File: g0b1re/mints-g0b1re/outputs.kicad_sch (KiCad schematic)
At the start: 46 parts, among them Q201 DMP3050LVT-7, Q202 DMP3050LVT-7, Q203 DMP3050LVT-7, Q204 DMP3050LVT-7, Q205 DMP3050LVT-7, Q206 DMP3050LVT-7, Q207 DMP3050LVT-7, Q208 DMP3050LVT-7, U201 140357145200, U202 140357145200, U203 140357145200, U204 140357145200, U205 140357145200, U206 140357145200, U207 140357145200, U208 140357145200

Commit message: notes from DR
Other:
- note added: "Add aux power LED"
- note added: "pick better fet P channel MOSFET 60v 15A lowest on resistance you can"
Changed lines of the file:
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@@
+		)
+	)
+	(text "Add aux power LED"
+		(exclude_from_sim no)
+		(at 270.256 78.74 0)
+		(effects
+			(font
+				(size 1.27 1.27)
+				(color 255 29 20 1)
+			)
 		)
 	)
@@
 			(font
 				(size 1.27 1.27)
+			)
+		)
+	)
+	(text "pick better fet\nP channel MOSFET\n60v 15A\nlowest on resistance you can"
+		(exclude_from_sim no)
+		(at 195.58 46.99 0)
+		(effects
+			(font
+				(size 1.27 1.27)
+				(color 255 25 18 1)
 			)
 		)
@@
 			(justify left bottom)
 		)
-		(property "Netclass" "iso_power"
+		(property "Net Class" "iso_power"
 			(at 309.8165 76.47 0)
 			(show_name no)
@@
 			(justify left bottom)
 		)
-		(property "Netclass" "data"
+		(property "Net Class" "data"
 			(at 119.3165 61.23 0)
 			(show_name no)
@@
 			(justify left bottom)
 		)
-		(property "Netclass" "data"
+		(property "Net Class" "data"
 			(at 119.3165 145.05 0)
 			(show_name no)
@@
 			(justify left bottom)
 		)
-		(property "Netclass" "data"
+		(property "Net Class" "data"
 			(at 119.3165 103.14 0)
 			(show_name no)
@@
 			(justify left bottom)
 		)
-		(property "Netclass" "iso_power"
+		(property "Net Class" "iso_power"
 			(at 288.2265 79.01 0)
 			(show_name no)
@@
 			(justify left bottom)
 		)
-		(property "Netclass" "data"
+		(property "Net Class" "data"
 			(at 119.3165 81.55 0)
 			(show_name no)
@@
 			(justify left bottom)
 		)
-		(property "Netclass" "data"
+		(property "Net Class" "data"
 			(at 119.3165 165.37 0)
 			(show_name no)
@@
 			(justify left bottom)
 		)
-		(property "Netclass" "iso_power"
+		(property "Net Class" "iso_power"
 			(at 288.2265 76.47 0)
 			(show_name no)
@@
 			(justify left bottom)
 		)
-		(property "Netclass" "data"
+		(property "Net Class" "data"
 			(at 119.3165 186.96 0)
 			(show_name no)
@@
 			(justify left bottom)
 		)
-		(property "Netclass" "data"
+		(property "Net Class" "data"
 			(at 119.3165 123.46 0)
 			(show_name no)
@@
 			(justify left bottom)
 		)
-		(property "Netclass" "data"
+		(property "Net Class" "data"
 			(at 119.3165 207.28 0)
 			(show_name no)

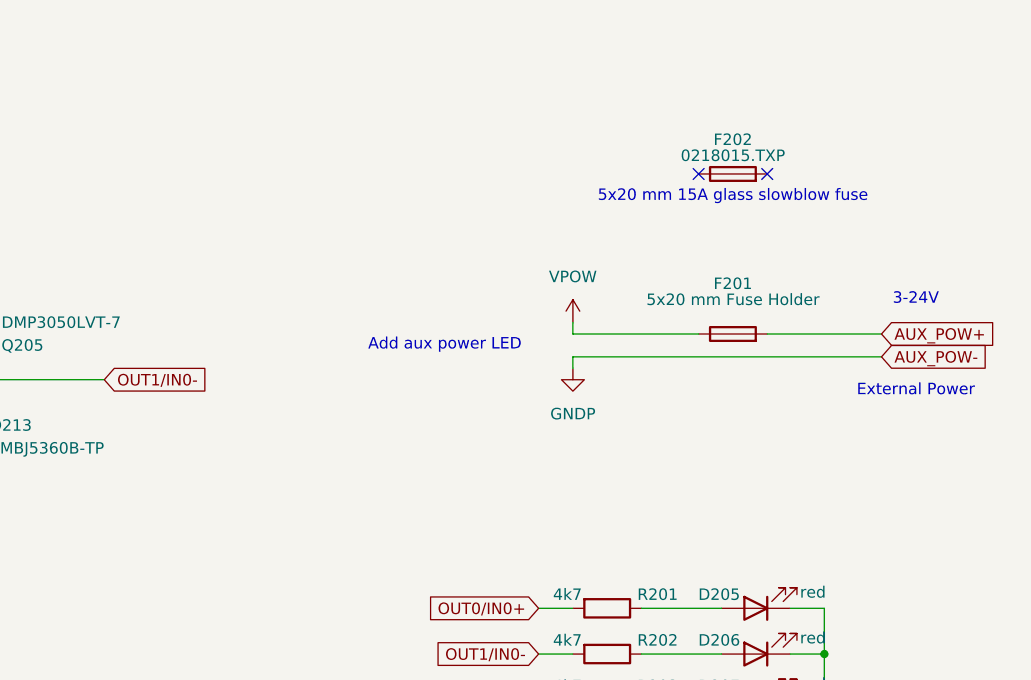
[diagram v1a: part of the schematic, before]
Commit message: post board review schmatic updates
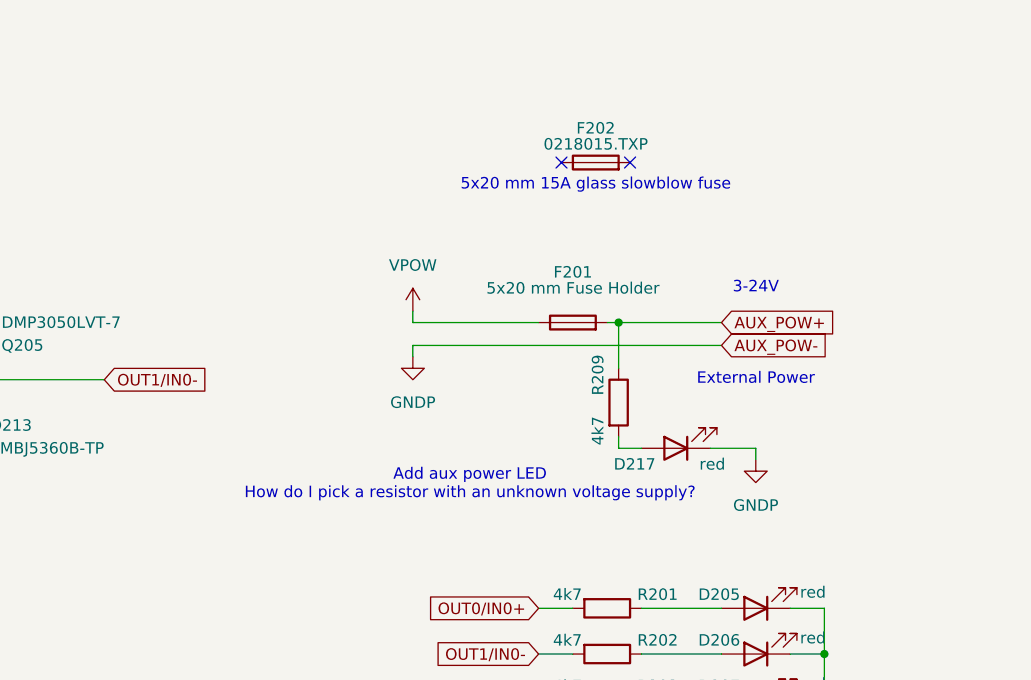
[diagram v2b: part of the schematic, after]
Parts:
- added D217: red, LED_SMD:LED_0603_1608Metric, symbol Device:LED
- added R209: 4k7, Resistor_SMD:R_0603_1608Metric, symbol Device:R
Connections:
- net AUX_POW+: now also R209.1
- net GNDP: now also D217.1 (K)
- new net: D217.2 (A), R209.2
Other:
- note added: "Add aux power LED How do I pick a resistor with an unknown voltage supply?"
- note removed: "Add aux power LED"
- moved on the sheet: F201, F202

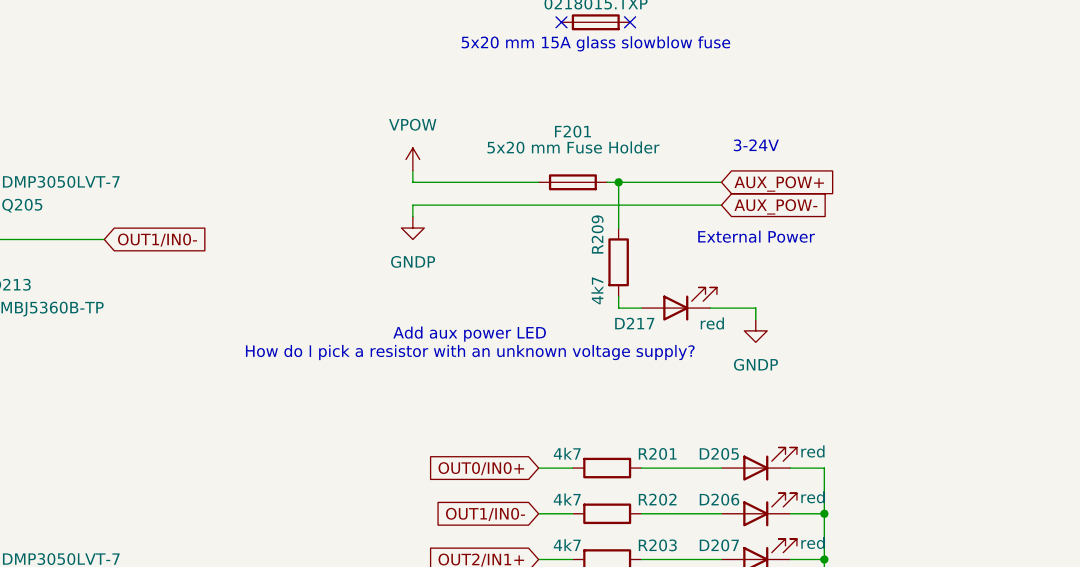
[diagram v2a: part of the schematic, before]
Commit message: Schematic progress
Swapped s2c chip, changed 8 pin connecters out with 4 pin, added test
point, removed net labels
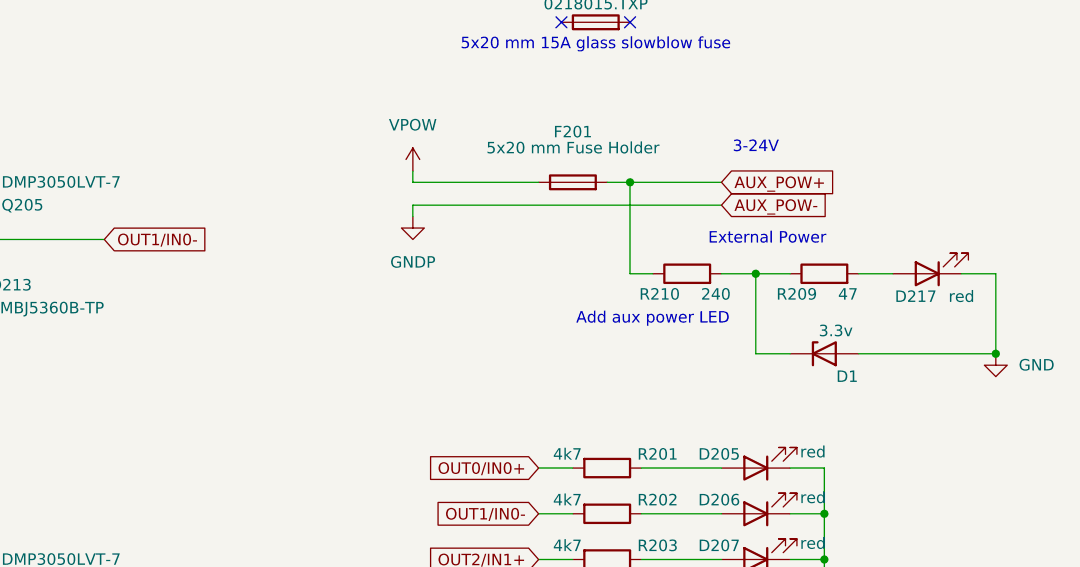
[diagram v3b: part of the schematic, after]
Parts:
- added D1: 3.3v, symbol Device:D_Zener
- added R210: 240, Resistor_SMD:R_0603_1608Metric, symbol Device:R
- R209: value 4k7 -> 47
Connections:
- net AUX_POW+: now also R210.1; no longer R209.1
- net GND: now also D217.1 (K), D1.2 (A)
- net GNDP: no longer D217.1 (K)
- new net: D1.1 (K), R209.1, R210.2
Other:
- note added: "Add aux power LED"
- note removed: "Add aux power LED How do I pick a resistor with an unknown voltage supply?"
- moved on the sheet: D217, R209

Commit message: Finished Schematic
Added STLINK header. Added flash header. Changed ADC. Fixed ESD caps.
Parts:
- removed Q201, Q202, Q203, Q204, Q205, Q206, Q207, Q208: DMP3050LVT-7, Package_TO_SOT_SMD:TSOT-23-6, symbol oresat-transistors:DMP3050LVT-7
- added Q1, Q2, Q3, Q4, Q5, Q6, Q7, Q8: SQM120P06-07L_GE3, TO-263_SQM120P06-07L_GE3_VIS, symbol 2026-07-27_21-07-26:SQM120P06-07L_GE3
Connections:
- net OUT0/IN0+: now also Q1.3 (S)
- net OUT1/IN0-: now also Q2.3 (S)
- net OUT2/IN1+: now also Q3.3 (S)
- net OUT3/IN1-: now also Q8.3 (S)
- net OUT4/IN2+: now also Q4.3 (S)
- net OUT5/IN2-: now also Q5.3 (S)
- net OUT6/IN3+: now also Q6.3 (S)
- net OUT7/IN3-: now also Q7.3 (S)
- net VPOW: now also Q1.2 (D), Q2.2 (D), Q3.2 (D), Q4.2 (D), Q5.2 (D), Q6.2 (D), Q7.2 (D), Q8.2 (D)
- net ~{ISO_OUT_0}: now also Q1.1 (G)
- net ~{ISO_OUT_1}: now also Q2.1 (G)
- net ~{ISO_OUT_2}: now also Q3.1 (G)
- net ~{ISO_OUT_3}: now also Q8.1 (G)
- net ~{ISO_OUT_4}: now also Q4.1 (G)
- net ~{ISO_OUT_5}: now also Q5.1 (G)
- net ~{ISO_OUT_6}: now also Q6.1 (G)
- net ~{ISO_OUT_7}: now also Q7.1 (G)
